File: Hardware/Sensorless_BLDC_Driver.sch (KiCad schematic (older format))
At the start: 66 parts, among them J1 POWER, J2 MOTOR, Q1 BUK7M15-60EX, Q2 BUK7M15-60EX, Q3 BUK7M15-60EX, Q4 BUK7M15-60EX, Q5 BUK7M15-60EX, Q6 BUK7M15-60EX, U1 PSoC5LP_Prototyping_Kit, U2 FAN7888

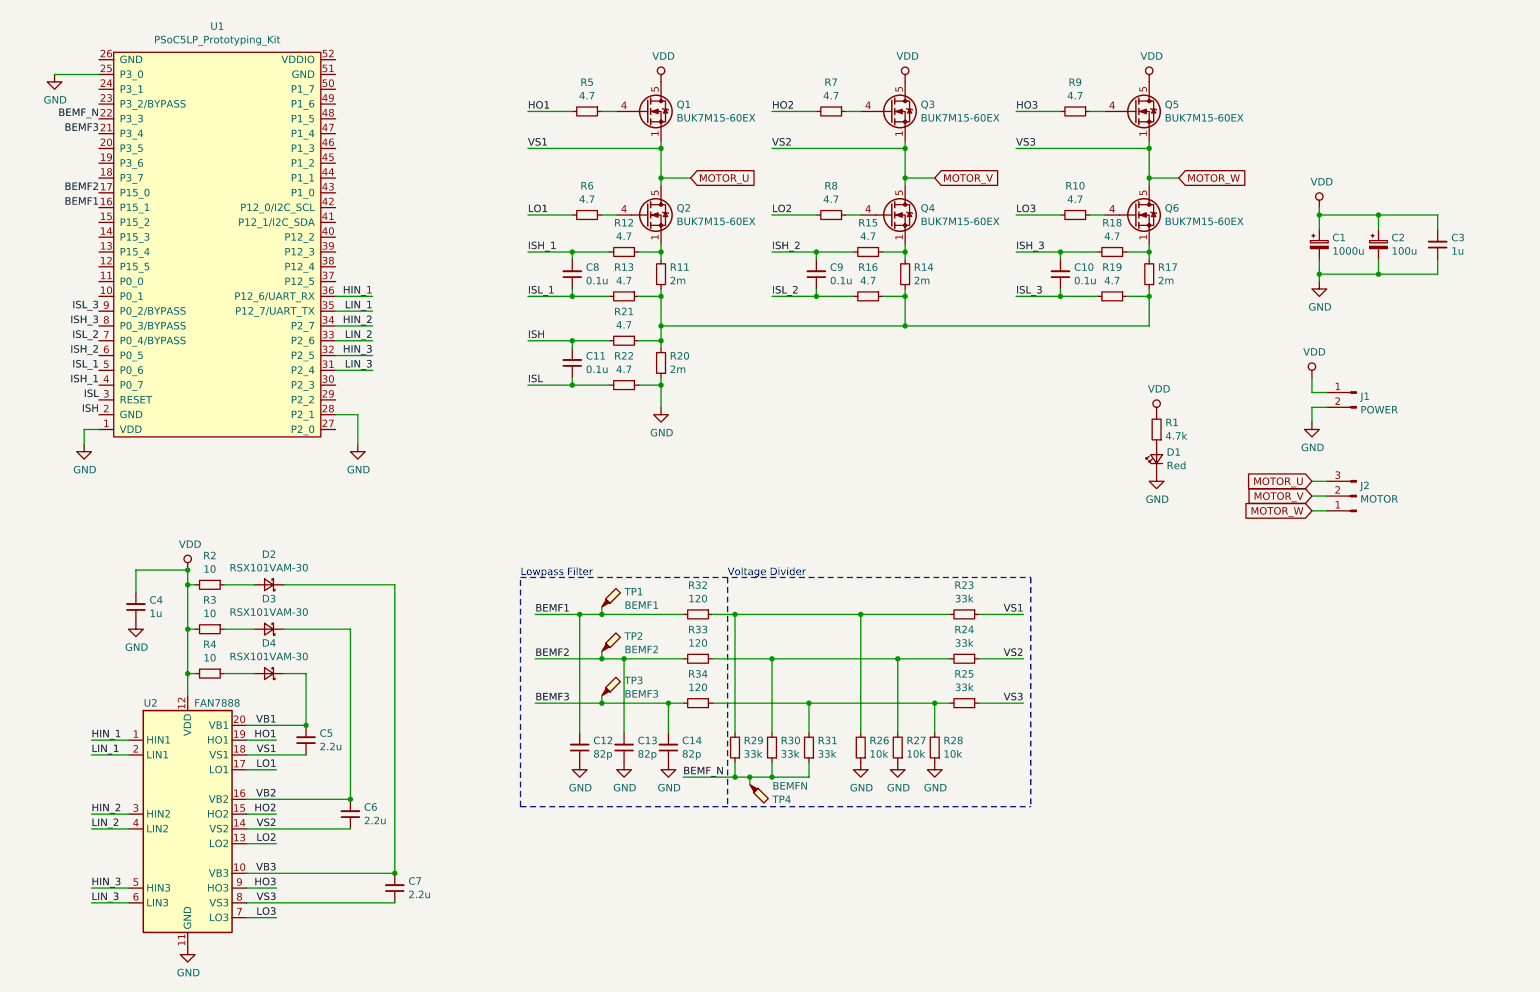
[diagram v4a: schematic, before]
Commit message: [add] assign footprint
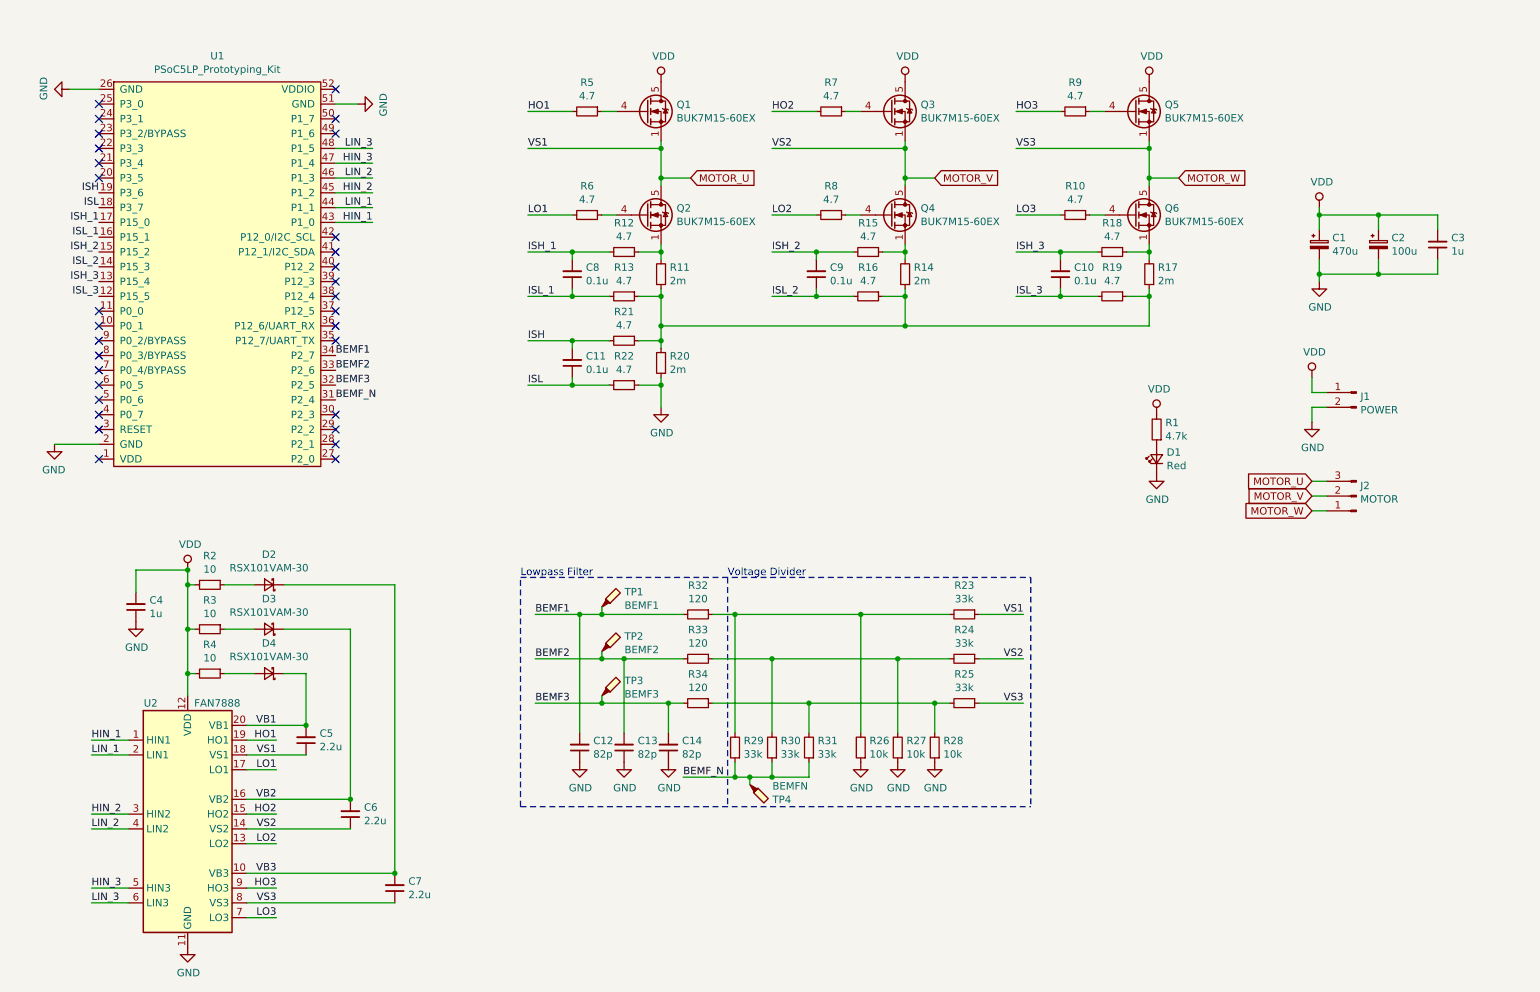
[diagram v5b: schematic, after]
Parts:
- C1: value 1000u -> 470u; footprint (none) -> Capacitor_SMD:CP_Elec_10x10; Agency (none) -> Digikey
- C10, C11, C8, C9: footprint (none) -> Capacitor_SMD:C_0402_1005Metric; Agency (none) -> Digikey; Link (none) -> https://www.digikey.jp/product-detail/ja/murata-electronics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; MPN (none) -> GRM155R62A104KE14D
- C12, C13, C14: footprint (none) -> Capacitor_SMD:C_0402_1005Metric; Agency (none) -> mouser; Link (none) -> https://www.mouser.jp/ProductDetail/Murata-Electronics/GRM1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; MPN (none) -> GRM1555C1H820JA01D
- C2: footprint (none) -> Capacitor_SMD:CP_Elec_6.3x7.7; Agency (none) -> DIgikey; Link (none) -> https://www.digikey.jp/product-detail/ja/nichicon/UWT1E471M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; MPN (none) -> UWT1E471MNL1GS
- C3, C4: footprint (none) -> Capacitor_SMD:C_0402_1005Metric; Agency (none) -> Digikey; Link (none) -> https://www.digikey.jp/product-detail/ja/murata-electronics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; MPN (none) -> GRM155R61E105KA12D
- C5, C6, C7: footprint (none) -> Capacitor_SMD:C_0603_1608Metric; Agency (none) -> mouser; Link (none) -> https://www.mouser.jp/ProductDetail/Murata-Electronics/GRM1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; MPN (none) -> GRM188R61E225MA12D
- D1: footprint (none) -> LED_SMD:LED_0603_1608Metric
- D2, D3, D4: footprint (none) -> Diode_SMD:D_TUMD2; Agency (none) -> akizuki; Link (none) -> http://akizukidenshi.com/catalog/g/gI-05951/; MPN (none) -> RSX101VAM-30TR
- J1: footprint (none) -> Connector_Hirose:Hirose_DF63M-2P-3.96DSA_1x02_P3.96mm_Vertical; Agency (none) -> mouser; Link (none) -> https://www.mouser.jp/ProductDetail/Hirose-Connector/DF63M-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; MPN (none) -> DF63M-2P-3.96DSA
- J2: footprint (none) -> Connector_Hirose:Hirose_DF63M-3P-3.96DSA_1x03_P3.96mm_Vertical; Agency (none) -> mouser; Link (none) -> https://www.mouser.jp/ProductDetail/Hirose-Connector/DF63M-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; MPN (none) -> DF63M-3P-3.96DSA
- R1: footprint (none) -> Resistor_SMD:R_0402_1005Metric; Agency (none) -> Digkey; Link (none) -> https://www.digikey.jp/product-detail/ja/panasonic-electron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; MPN (none) -> ERJ-2GEJ472X
- R10, R12, R13, R15, R16, R18, R19, R21, R22, R5, R6, R7, R8, R9: footprint (none) -> Resistor_SMD:R_0402_1005Metric; Agency (none) -> Digkey; Link (none) -> https://www.digikey.jp/product-detail/ja/panasonic-electron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; MPN (none) -> ERJ-2GEJ4R7X
- R11, R14, R17, R20: footprint (none) -> Resistor_SMD:R_0805_2012Metric; Agency (none) -> Digikey; Link (none) -> https://www.digikey.jp/product-detail/ja/rohm-semiconductor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; MPN (none) -> PMR10EZPFV2L00
- R2, R3, R4: footprint (none) -> Resistor_SMD:R_0402_1005Metric; Agency (none) -> mouser; Link (none) -> https://www.mouser.jp/ProductDetail/Panasonic/ERJ-2RKF10R0X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; MPN (none) -> ERJ-2RKF10R0X
- R23, R24, R25, R29, R30, R31: footprint (none) -> Resistor_SMD:R_0402_1005Metric; Agency (none) -> mouser; Link (none) -> https://www.mouser.jp/ProductDetail/Panasonic/ERJ-2RKF3302X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; MPN (none) -> ERJ-2RKF3302X
- R26, R27, R28: footprint (none) -> Resistor_SMD:R_0402_1005Metric; Agency (none) -> Digikey; Link (none) -> https://www.digikey.jp/product-detail/ja/panasonic-electron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; MPN (none) -> ERJ-2GEJ103X
- R32, R33, R34: footprint (none) -> Resistor_SMD:R_0402_1005Metric; Agency (none) -> mouser; Link (none) -> https://www.mouser.jp/ProductDetail/Panasonic/ERJ-2RKF1200X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; MPN (none) -> ERJ-2RKF1200X
- U1: footprint (none) -> KUTKiCad_footprint:CY8CKIT-059
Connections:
- net BEMF1: now also U1.34 (P2_7); no longer U1.16 (P15_1)
- net BEMF2: now also U1.33 (P2_6); no longer U1.17 (P15_0)
- net BEMF3: now also U1.32 (P2_5); no longer U1.21 (P3_4)
- net BEMF_N: now also U1.31 (P2_4); no longer U1.22 (P3_3)
- net GND: now also U1.2 (GND), U1.26 (GND), U1.51 (GND); no longer U1.1 (VDD), U1.25 (P3_0), U1.28 (P2_1)
- net HIN_1: now also U1.43 (P1_0); no longer U1.36 (P12_6/UART_RX)
- net HIN_2: now also U1.45 (P1_2); no longer U1.34 (P2_7)
- net HIN_3: now also U1.47 (P1_4); no longer U1.32 (P2_5)
- net ISH: now also U1.19 (P3_6); no longer U1.2 (GND)
- net ISH_1: now also U1.17 (P15_0); no longer U1.4 (P0_7)
- net ISH_2: now also U1.15 (P15_2); no longer U1.6 (P0_5)
- net ISH_3: now also U1.13 (P15_4); no longer U1.8 (P0_3/BYPASS)
- net ISL: now also U1.18 (P3_7); no longer U1.3 (RESET)
- net ISL_1: now also U1.16 (P15_1); no longer U1.5 (P0_6)
- net ISL_2: now also U1.14 (P15_3); no longer U1.7 (P0_4/BYPASS)
- net ISL_3: now also U1.12 (P15_5); no longer U1.9 (P0_2/BYPASS)
- net LIN_1: now also U1.44 (P1_1); no longer U1.35 (P12_7/UART_TX)
- net LIN_2: now also U1.46 (P1_3); no longer U1.33 (P2_6)
- net LIN_3: now also U1.48 (P1_5); no longer U1.31 (P2_4)
- no-connect marks 0 -> 31

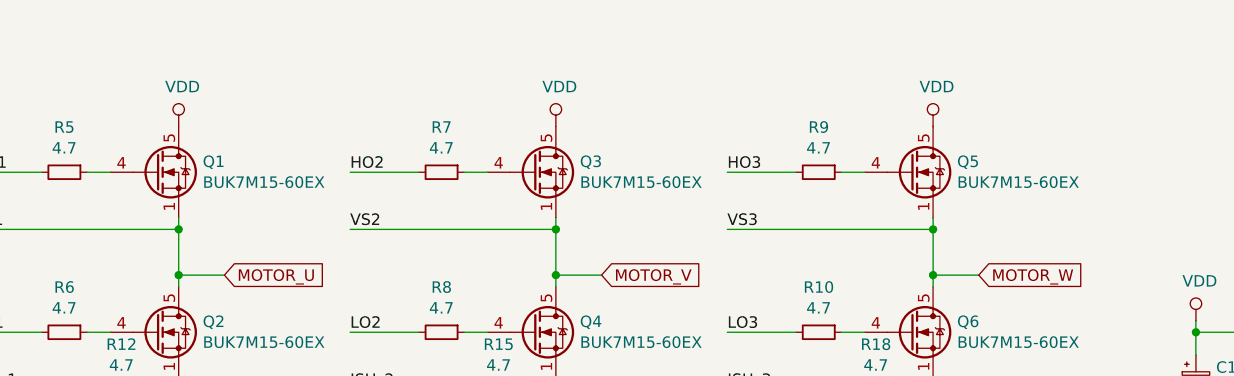
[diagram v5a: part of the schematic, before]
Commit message: [add] add VDD pass capacitor
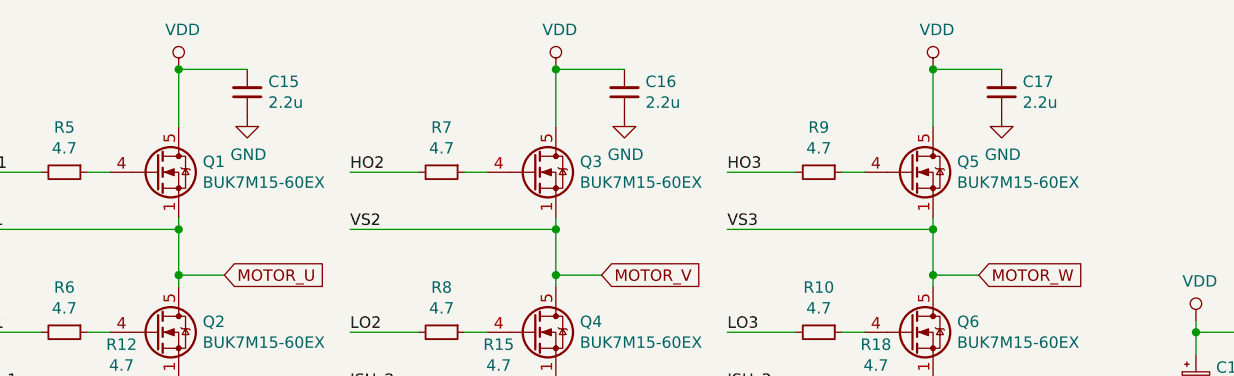
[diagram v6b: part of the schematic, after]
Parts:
- added C15, C16, C17: 2.2u, Capacitor_SMD:C_0603_1608Metric, symbol Device:C_Small
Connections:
- net GND: now also C15.1, C16.1, C17.1
- net VDD: now also C15.2, C16.2, C17.2
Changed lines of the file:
@@
 	5350 1400 5350 1450
-$Comp
-L power:VDD #PWR0102
-U 1 1 5EA87D73
-P 5350 1000
-F 0 "#PWR0102" H 5350 850 50  0001 C CNN
-F 1 "VDD" H 5367 1173 50  0000 C CNN
-F 2 "" H 5350 1000 50  0001 C CNN
-F 3 "" H 5350 1000 50  0001 C CNN
-	1    5350 1000
-	1    0    0    -1
-$EndComp
 $Comp
 L Transistor_FET:BUK7M15-60EX Q3
@@
 	7000 1400 7000 1450
 $Comp
-L power:VDD #PWR0103
-U 1 1 5EA892B0
-P 7000 1000
-F 0 "#PWR0103" H 7000 850 50  0001 C CNN
-F 1 "VDD" H 7017 1173 50  0000 C CNN
-F 2 "" H 7000 1000 50  0001 C CNN
-F 3 "" H 7000 1000 50  0001 C CNN
-	1    7000 1000
-	1    0    0    -1
-$EndComp
-$Comp
 L Transistor_FET:BUK7M15-60EX Q5
 U 1 1 5EA8A514
@@
 L power:VDD #PWR0104
 U 1 1 5EA8A53E
-P 8650 1000
-F 0 "#PWR0104" H 8650 850 50  0001 C CNN
-F 1 "VDD" H 8667 1173 50  0000 C CNN
-F 2 "" H 8650 1000 50  0001 C CNN
-F 3 "" H 8650 1000 50  0001 C CNN
-	1    8650 1000
+P 8650 750
+F 0 "#PWR0104" H 8650 600 50  0001 C CNN
+F 1 "VDD" H 8667 923 50  0000 C CNN
+F 2 "" H 8650 750 50  0001 C CNN
+F 3 "" H 8650 750 50  0001 C CNN
+	1    8650 750
 	1    0    0    -1
 $EndComp
@@
 NoConn ~ 3150 3450
 NoConn ~ 3150 3550
+Wire Wire Line
+	8650 1000 8650 750
+Wire Wire Line
+	8650 750  8950 750
+Connection ~ 8650 750
+$Comp
+L power:GND #PWR?
+U 1 1 5EC07216
+P 8950 950
+F 0 "#PWR?" H 8950 700 50  0001 C CNN
+F 1 "GND" H 8955 777 50  0000 C CNN
+F 2 "" H 8950 950 50  0001 C CNN
+F 3 "" H 8950 950 50  0001 C CNN
+	1    8950 950
+	1    0    0    -1
+$EndComp
+$Comp
+L power:VDD #PWR?
+U 1 1 5EC07660
+P 7000 750
+F 0 "#PWR?" H 7000 600 50  0001 C CNN
+F 1 "VDD" H 7017 923 50  0000 C CNN
+F 2 "" H 7000 750 50  0001 C CNN
+F 3 "" H 7000 750 50  0001 C CNN
+	1    7000 750
+	1    0    0    -1
+$EndComp
+Wire Wire Line
+	7000 1000 7000 750
+Wire Wire Line
+	7000 750  7300 750
+Connection ~ 7000 750
+$Comp
+L power:GND #PWR?
+U 1 1 5EC07673
+P 7300 950
+F 0 "#PWR?" H 7300 700 50  0001 C CNN
+F 1 "GND" H 7305 777 50  0000 C CNN
+F 2 "" H 7300 950 50  0001 C CNN
+F 3 "" H 7300 950 50  0001 C CNN
+	1    7300 950
+	1    0    0    -1
+$EndComp
+$Comp
+L power:VDD #PWR?
+U 1 1 5EC111A3
+P 5350 750
+F 0 "#PWR?" H 5350 600 50  0001 C CNN
+F 1 "VDD" H 5367 923 50  0000 C CNN
+F 2 "" H 5350 750 50  0001 C CNN
+F 3 "" H 5350 750 50  0001 C CNN
+	1    5350 750
+	1    0    0    -1
+$EndComp
+Wire Wire Line
+	5350 1000 5350 750
+Wire Wire Line
+	5350 750  5650 750
+Connection ~ 5350 750
+$Comp
+L power:GND #PWR?
+U 1 1 5EC111B6
+P 5650 950
+F 0 "#PWR?" H 5650 700 50  0001 C CNN
+F 1 "GND" H 5655 777 50  0000 C CNN
+F 2 "" H 5650 950 50  0001 C CNN
+F 3 "" H 5650 950 50  0001 C CNN
+	1    5650 950
+	1    0    0    -1
+$EndComp
+$Comp
+L Device:C_Small C15
+U 1 1 5EC257BC
+P 5650 850
+F 0 "C15" H 5558 804 50  0000 R CNN
+F 1 "2.2u" H 5558 895 50  0000 R CNN
+F 2 "Capacitor_SMD:C_0603_1608Metric" H 5650 850 50  0001 C CNN
+F 3 "https://www.mouser.jp/datasheet/2/281/murata_03052018_GRM_Series_1-1310166.pdf" H 5650 850 50  0001 C CNN
+F 4 "mouser" H 2700 -4600 50  0001 C CNN "Agency"
+F 5 "https://www.mouser.jp/ProductDetail/Murata-Electronics/GRM188R61E225MA12D?qs=sGAEpiMZZMuMW9TJLBQkXvhLBzZSIyMlqD0jXVqmhlI%3D" H 2700 -4600 50  0001 C CNN "Link"
+F 6 "GRM188R61E225MA12D" H 2700 -4600 50  0001 C CNN "MPN"
+	1    5650 850
+	-1   0    0    1
+$EndComp
+$Comp
+L Device:C_Small C16
+U 1 1 5EC25AEF
+P 7300 850
+F 0 "C16" H 7208 804 50  0000 R CNN
+F 1 "2.2u" H 7208 895 50  0000 R CNN
+F 2 "Capacitor_SMD:C_0603_1608Metric" H 7300 850 50  0001 C CNN
+F 3 "https://www.mouser.jp/datasheet/2/281/murata_03052018_GRM_Series_1-1310166.pdf" H 7300 850 50  0001 C CNN
+F 4 "mouser" H 4350 -4600 50  0001 C CNN "Agency"
+F 5 "https://www.mouser.jp/ProductDetail/Murata-Electronics/GRM188R61E225MA12D?qs=sGAEpiMZZMuMW9TJLBQkXvhLBzZSIyMlqD0jXVqmhlI%3D" H 4350 -4600 50  0001 C CNN "Link"
+F 6 "GRM188R61E225MA12D" H 4350 -4600 50  0001 C CNN "MPN"
+	1    7300 850
+	-1   0    0    1
+$EndComp
+$Comp
+L Device:C_Small C17
+U 1 1 5EC25BB5
+P 8950 850
+F 0 "C17" H 8858 804 50  0000 R CNN
+F 1 "2.2u" H 8858 895 50  0000 R CNN
+F 2 "Capacitor_SMD:C_0603_1608Metric" H 8950 850 50  0001 C CNN
+F 3 "https://www.mouser.jp/datasheet/2/281/murata_03052018_GRM_Series_1-1310166.pdf" H 8950 850 50  0001 C CNN
+F 4 "mouser" H 6000 -4600 50  0001 C CNN "Agency"
+F 5 "https://www.mouser.jp/ProductDetail/Murata-Electronics/GRM188R61E225MA12D?qs=sGAEpiMZZMuMW9TJLBQkXvhLBzZSIyMlqD0jXVqmhlI%3D" H 6000 -4600 50  0001 C CNN "Link"
+F 6 "GRM188R61E225MA12D" H 6000 -4600 50  0001 C CNN "MPN"
+	1    8950 850
+	-1   0    0    1
+$EndComp
 $EndSCHEMATC
